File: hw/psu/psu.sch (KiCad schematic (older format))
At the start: 101 parts, among them J1 BATTERY, J2 CAN, J3 DEBUG, J4 SWD, J5 SDU, J6 HMI, J7 ECU, U1 INA180A1, U2 MCP2562-E-SN, U3 TS1117BCW33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

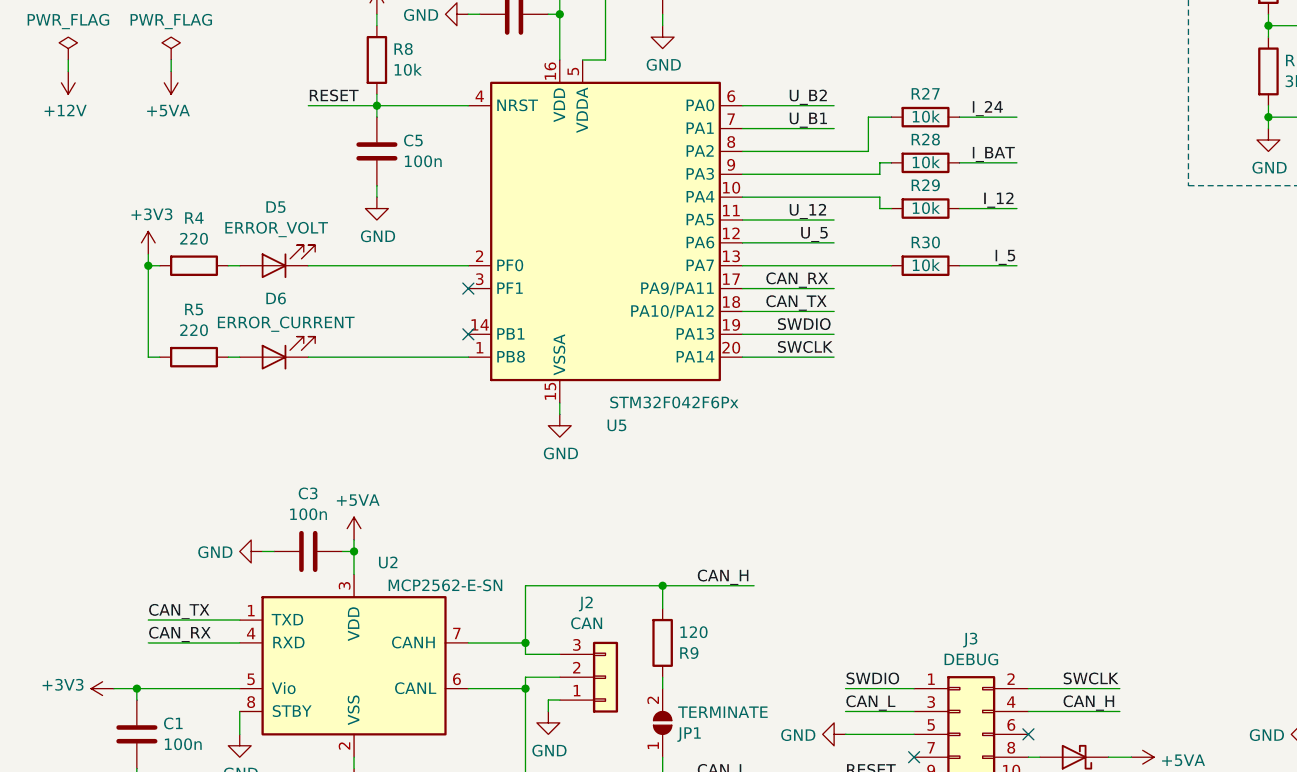
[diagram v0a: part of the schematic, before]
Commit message: Added crystal for all can equipped boards
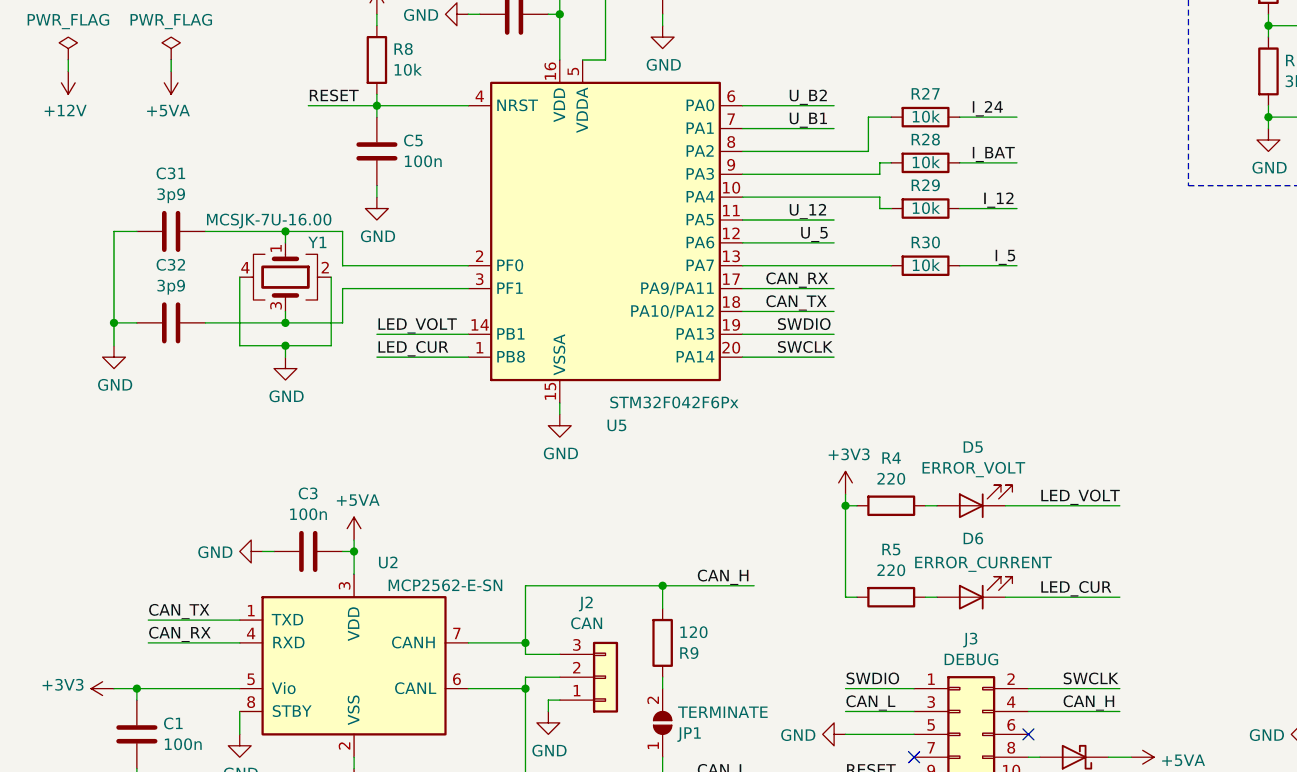
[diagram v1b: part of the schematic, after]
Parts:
- added C31, C32: 3p9, Capacitor_SMD:C_0805_2012Metric, symbol Device:C
- added Y1: MCSJK-7U-16.00, Crystal:Crystal_SMD_3225-4Pin_3.2x2.5mm, symbol Device:Crystal_GND24
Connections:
- net labels added: LED_CUR, LED_VOLT
- wire segments 388 -> 409
- no-connect marks 7 -> 5
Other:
- moved on the sheet: D5, D6, R4, R5
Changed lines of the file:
@@
 Sheet 1 1
 Title "BUT Pneumobil - PSU"
-Date ""
-Rev "0.1"
+Date "2019-03-10"
+Rev "0.2"
 Comp "Brno University of Technology"
 Comment1 "Jakub Kaderka"
@@
 L Device:LED D5
 U 1 1 5C52E5B9
-P 1600 5300
-F 0 "D5" H 1592 5045 50  0000 C CNN
-F 1 "ERROR_VOLT" H 1592 5136 50  0000 C CNN
-F 2 "LED_SMD:LED_1206_3216Metric" H 1600 5300 50  0001 C CNN
-F 3 "~" H 1600 5300 50  0001 C CNN
-	1    1600 5300
+P 4650 6350
+F 0 "D5" H 4642 6095 50  0000 C CNN
+F 1 "ERROR_VOLT" H 4642 6186 50  0000 C CNN
+F 2 "LED_SMD:LED_1206_3216Metric" H 4650 6350 50  0001 C CNN
+F 3 "~" H 4650 6350 50  0001 C CNN
+	1    4650 6350
 	-1   0    0    1
 $EndComp
@@
 L Device:LED D6
 U 1 1 5C52E826
-P 1600 5700
-F 0 "D6" H 1592 5445 50  0000 C CNN
-F 1 "ERROR_CURRENT" H 1550 5550 50  0000 C CNN
-F 2 "LED_SMD:LED_1206_3216Metric" H 1600 5700 50  0001 C CNN
-F 3 "~" H 1600 5700 50  0001 C CNN
-	1    1600 5700
+P 4650 6750
+F 0 "D6" H 4642 6495 50  0000 C CNN
+F 1 "ERROR_CURRENT" H 4600 6600 50  0000 C CNN
+F 2 "LED_SMD:LED_1206_3216Metric" H 4650 6750 50  0001 C CNN
+F 3 "~" H 4650 6750 50  0001 C CNN
+	1    4650 6750
 	-1   0    0    1
 $EndComp
@@
 L Device:R R4
 U 1 1 5CABE61E
-P 1250 5300
-F 0 "R4" V 1043 5300 50  0000 C CNN
-F 1 "220" V 1134 5300 50  0000 C CNN
-F 2 "Resistor_SMD:R_0805_2012Metric" V 1180 5300 50  0001 C CNN
-F 3 "~" H 1250 5300 50  0001 C CNN
-	1    1250 5300
-	0    1    1    0
-$EndComp
-Wire Wire Line
-	1400 5300 1450 5300
+P 4300 6350
+F 0 "R4" V 4093 6350 50  0000 C CNN
+F 1 "220" V 4184 6350 50  0000 C CNN
+F 2 "Resistor_SMD:R_0805_2012Metric" V 4230 6350 50  0001 C CNN
+F 3 "~" H 4300 6350 50  0001 C CNN
+	1    4300 6350
+	0    1    1    0
+$EndComp
+Wire Wire Line
+	4450 6350 4500 6350
 $Comp
 L Device:R R5
 U 1 1 5CAD67F2
-P 1250 5700
-F 0 "R5" V 1043 5700 50  0000 C CNN
-F 1 "220" V 1134 5700 50  0000 C CNN
-F 2 "Resistor_SMD:R_0805_2012Metric" V 1180 5700 50  0001 C CNN
-F 3 "~" H 1250 5700 50  0001 C CNN
-	1    1250 5700
-	0    1    1    0
-$EndComp
-Wire Wire Line
-	1400 5700 1450 5700
-Wire Wire Line
-	1100 5700 1050 5700
-Wire Wire Line
-	1050 5700 1050 5300
-Wire Wire Line
-	1100 5300 1050 5300
-Connection ~ 1050 5300
-Wire Wire Line
-	1050 5300 1050 5250
+P 4300 6750
+F 0 "R5" V 4093 6750 50  0000 C CNN
+F 1 "220" V 4184 6750 50  0000 C CNN
+F 2 "Resistor_SMD:R_0805_2012Metric" V 4230 6750 50  0001 C CNN
+F 3 "~" H 4300 6750 50  0001 C CNN
+	1    4300 6750
+	0    1    1    0
+$EndComp
+Wire Wire Line
+	4450 6750 4500 6750
+Wire Wire Line
+	4150 6750 4100 6750
+Wire Wire Line
+	4100 6750 4100 6350
+Wire Wire Line
+	4150 6350 4100 6350
+Connection ~ 4100 6350
+Wire Wire Line
+	4100 6350 4100 6300
 $Comp
 L power:+3V3 #PWR08
 U 1 1 5CB50E5E
-P 1050 5250
-F 0 "#PWR08" H 1050 5100 50  0001 C CNN
-F 1 "+3V3" H 1065 5423 50  0000 C CNN
-F 2 "" H 1050 5250 50  0001 C CNN
-F 3 "" H 1050 5250 50  0001 C CNN
-	1    1050 5250
+P 4100 6300
+F 0 "#PWR08" H 4100 6150 50  0001 C CNN
+F 1 "+3V3" H 4115 6473 50  0000 C CNN
+F 2 "" H 4100 6300 50  0001 C CNN
+F 3 "" H 4100 6300 50  0001 C CNN
+	1    4100 6300
 	1    0    0    -1
 $EndComp
@@
 $EndComp
 Wire Wire Line
-	1750 5700 2450 5700
-Wire Wire Line
-	1750 5300 2450 5300
+	4800 6750 5300 6750
 $Comp
 L Device:D D7
@@
 Wire Wire Line
 	9600 6100 9950 6100
-NoConn ~ 2450 5400
 Wire Wire Line
 	3500 1700 3500 1800
@@
 Wire Wire Line
 	2850 4200 2850 4400
-NoConn ~ 2450 5600
 $Comp
 L Device:R R27
@@
 Wire Wire Line
 	4300 5300 3650 5300
+Wire Wire Line
+	4800 6350 5300 6350
+$Comp
+L Device:Crystal_GND24 Y1
+U 1 1 5C90194C
+P 1650 5350
+F 0 "Y1" V 1500 5450 50  0000 L CNN
+F 1 "MCSJK-7U-16.00" V 1400 5000 50  0000 L CNN
+F 2 "Crystal:Crystal_SMD_3225-4Pin_3.2x2.5mm" H 1650 5350 50  0001 C CNN
+F 3 "~" H 1650 5350 50  0001 C CNN
+	1    1650 5350
+	0    1    1    0
+$EndComp
+Wire Wire Line
+	1850 5350 1850 5650
+Wire Wire Line
+	1850 5650 1650 5650
+Wire Wire Line
+	1450 5650 1450 5350
+$Comp
+L power:GND #PWR065
+U 1 1 5CA63F51
+P 1650 5700
+F 0 "#PWR065" H 1650 5450 50  0001 C CNN
+F 1 "GND" H 1655 5527 50  0000 C CNN
+F 2 "" H 1650 5700 50  0001 C CNN
+F 3 "" H 1650 5700 50  0001 C CNN
+	1    1650 5700
+	1    0    0    -1
+$EndComp
+Wire Wire Line
+	1650 5700 1650 5650
+Connection ~ 1650 5650
+Wire Wire Line
+	1650 5650 1450 5650
+Wire Wire Line
+	2450 5300 1900 5300
+Wire Wire Line
+	1900 5300 1900 5150
+Wire Wire Line
+	1900 5150 1650 5150
+Wire Wire Line
+	1650 5150 1650 5200
+Wire Wire Line
+	2450 5400 1900 5400
+Wire Wire Line
+	1900 5400 1900 5550
+Wire Wire Line
+	1900 5550 1650 5550
+Wire Wire Line
+	1650 5550 1650 5500
+$Comp
+L Device:C C31
+U 1 1 5CB44DD2
+P 1150 5150
+F 0 "C31" V 898 5150 50  0000 C CNN
+F 1 "3p9" V 989 5150 50  0000 C CNN
+F 2 "Capacitor_SMD:C_0805_2012Metric" H 1188 5000 50  0001 C CNN
+F 3 "~" H 1150 5150 50  0001 C CNN
+	1    1150 5150
+	0    1    1    0
+$EndComp
+$Comp
+L Device:C C32
+U 1 1 5CB450ED
+P 1150 5550
+F 0 "C32" V 898 5550 50  0000 C CNN
+F 1 "3p9" V 989 5550 50  0000 C CNN
+F 2 "Capacitor_SMD:C_0805_2012Metric" H 1188 5400 50  0001 C CNN
+F 3 "~" H 1150 5550 50  0001 C CNN
+	1    1150 5550
+	0    1    1    0
+$EndComp
+Wire Wire Line
+	1650 5150 1300 5150
+Connection ~ 1650 5150
+Wire Wire Line
+	1650 5550 1300 5550
+Connection ~ 1650 5550
+$Comp
+L power:GND #PWR064
+U 1 1 5CBA1477
+P 900 5650
+F 0 "#PWR064" H 900 5400 50  0001 C CNN
+F 1 "GND" H 905 5477 50  0000 C CNN
+F 2 "" H 900 5650 50  0001 C CNN
+F 3 "" H 900 5650 50  0001 C CNN
+	1    900  5650
+	1    0    0    -1
+$EndComp
+Wire Wire Line
+	900  5650 900  5550
+Wire Wire Line
+	900  5150 1000 5150
+Wire Wire Line
+	1000 5550 900  5550
+Connection ~ 900  5550
+Wire Wire Line
+	900  5550 900  5150
+Wire Wire Line
+	2450 5600 2050 5600
+Text Label 2050 5600 0    50   ~ 0
+LED_VOLT
+Wire Wire Line
+	2450 5700 2050 5700
+Text Label 2050 5700 0    50   ~ 0
+LED_CUR
+Text Label 4950 6350 0    50   ~ 0
+LED_VOLT
+Text Label 4950 6750 0    50   ~ 0
+LED_CUR
 $EndSCHEMATC

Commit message: Fixed values of few components on psu board
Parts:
- C16, C17: value 100n -> 10n
- C19, C20: value 82p -> C
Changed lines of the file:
@@
 P 6350 850
 F 0 "C16" V 6098 850 50  0000 C CNN
-F 1 "100n" V 6189 850 50  0000 C CNN
+F 1 "10n" V 6189 850 50  0000 C CNN
 F 2 "Capacitor_SMD:C_0805_2012Metric" H 6388 700 50  0001 C CNN
 F 3 "~" H 6350 850 50  0001 C CNN
@@
 P 7700 1250
 F 0 "C19" H 7815 1296 50  0000 L CNN
-F 1 "82p" H 7815 1205 50  0000 L CNN
+F 1 "C" H 7815 1205 50  0000 L CNN
 F 2 "Capacitor_SMD:C_0805_2012Metric" H 7738 1100 50  0001 C CNN
 F 3 "~" H 7700 1250 50  0001 C CNN
@@
 P 6350 2300
 F 0 "C17" V 6098 2300 50  0000 C CNN
-F 1 "100n" V 6189 2300 50  0000 C CNN
+F 1 "10n" V 6189 2300 50  0000 C CNN
 F 2 "Capacitor_SMD:C_0805_2012Metric" H 6388 2150 50  0001 C CNN
 F 3 "~" H 6350 2300 50  0001 C CNN
@@
 P 7700 2700
 F 0 "C20" H 7815 2746 50  0000 L CNN
-F 1 "82p" H 7815 2655 50  0000 L CNN
+F 1 "C" H 7815 2655 50  0000 L CNN
 F 2 "Capacitor_SMD:C_0805_2012Metric" H 7738 2550 50  0001 C CNN
 F 3 "~" H 7700 2700 50  0001 C CNN

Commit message: Fixed diode polarity
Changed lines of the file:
@@
 F 3 "~" H 2700 2500 50  0001 C CNN
 	1    2700 2500
-	-1   0    0    1
+	1    0    0    -1
 $EndComp
 Wire Wire Line
